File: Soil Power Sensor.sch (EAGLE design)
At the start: 99 parts, among them J1 12401832E402A, U10 TPS7A20330PDBVR, U11 TPS60403DBVR, U12 REF1933AIDDCR, U13 TLV1117LV33DCYR, U14 FSA2466UMX, U2 FT234XD-R, U3 MAX9944ATA+T, U4 ESP32-C3-MINI-1-N4, U5 LTC6362CDDPBF, U6 LTC6362CDDPBF, U7 INA296A5, U8 MAX11201AEUB+, U9 MAX11201AEUB+, X1 SMA-142-0701-801/806

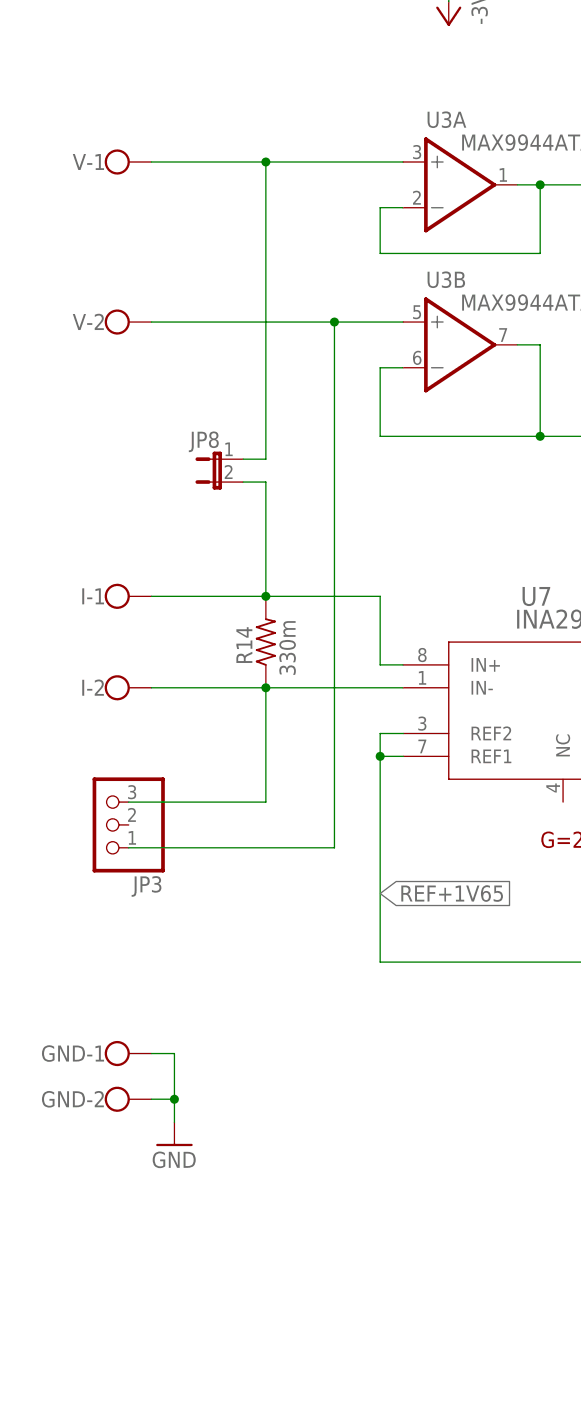
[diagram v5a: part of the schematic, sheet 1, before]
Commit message: Fixed in-situ load connections
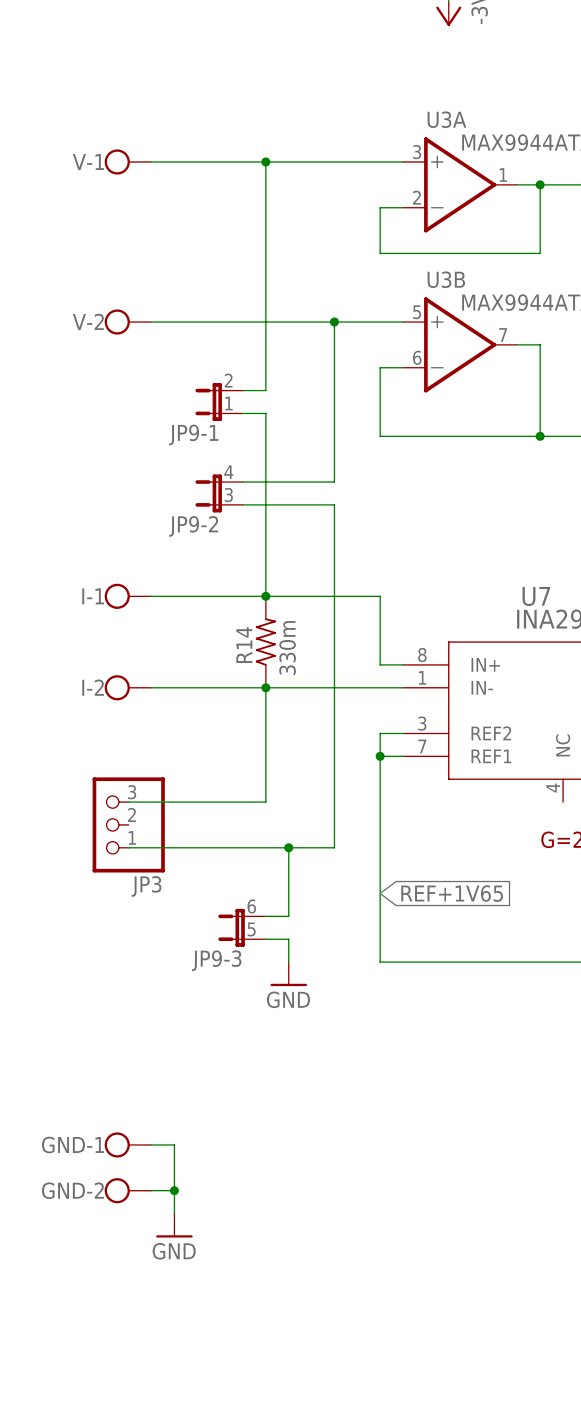
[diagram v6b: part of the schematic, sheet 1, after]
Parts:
- removed JP8: (no value), jumper:JP1E
- added JP9: (no value), jumper:JP3QE
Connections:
- new net N$48: JP3.1, JP9-2.1, JP9-3.2
- net GND: now also JP9-3.1
- net N$1: now also JP9-1.2; no longer JP8.1
- net N$45: now also JP9-1.1; no longer JP8.2
- net N$46: now also JP9-2.2; no longer JP3.1
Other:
- moved on the sheet: GND-1, GND-2
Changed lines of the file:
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@@
 <part name="V" library="con-wago-500" library_urn="urn:adsk.eagle:library:195" deviceset="W237-102" device="" package3d_urn="urn:adsk.eagle:package:10688/1"/>
 <part name="I" library="con-wago-500" library_urn="urn:adsk.eagle:library:195" deviceset="W237-102" device="" package3d_urn="urn:adsk.eagle:package:10688/1"/>
-<part name="JP8" library="jumper" library_urn="urn:adsk.eagle:library:252" deviceset="JP1E" device="" package3d_urn="urn:adsk.eagle:package:15455/1"/>
 <part name="JP2" library="jumper" library_urn="urn:adsk.eagle:library:252" deviceset="JP2E" device="" package3d_urn="urn:adsk.eagle:package:15452/1"/>
 <part name="P+7" library="supply1" library_urn="urn:adsk.eagle:library:371" deviceset="VCC" device=""/>
+<part name="JP9" library="jumper" library_urn="urn:adsk.eagle:library:252" deviceset="JP3QE" device="" package3d_urn="urn:adsk.eagle:package:15460/1"/>
+<part name="GND26" library="supply1" library_urn="urn:adsk.eagle:library:371" deviceset="GND" device=""/>
 </parts>
 <sheets>
@@
 <attribute name="TP_SIGNAL_NAME" x="95.25" y="97.79" size="1.778" layer="97"/>
 </instance>
-<instance part="GND" gate="-1" x="15.24" y="55.88" smashed="yes">
-<attribute name="NAME" x="15.24" y="56.769" size="1.778" layer="95" rot="R180"/>
-</instance>
-<instance part="GND" gate="-2" x="15.24" y="50.8" smashed="yes">
-<attribute name="VALUE" x="12.7" y="47.117" size="1.778" layer="96"/>
-<attribute name="NAME" x="15.24" y="51.689" size="1.778" layer="95" rot="R180"/>
-</instance>
-<instance part="GND42" gate="1" x="22.86" y="45.72" smashed="yes">
-<attribute name="VALUE" x="20.32" y="43.18" size="1.778" layer="96"/>
+<instance part="GND" gate="-1" x="15.24" y="45.72" smashed="yes">
+<attribute name="NAME" x="15.24" y="46.609" size="1.778" layer="95" rot="R180"/>
+</instance>
+<instance part="GND" gate="-2" x="15.24" y="40.64" smashed="yes">
+<attribute name="VALUE" x="12.7" y="36.957" size="1.778" layer="96"/>
+<attribute name="NAME" x="15.24" y="41.529" size="1.778" layer="95" rot="R180"/>
+</instance>
+<instance part="GND42" gate="1" x="22.86" y="35.56" smashed="yes">
+<attribute name="VALUE" x="20.32" y="33.02" size="1.778" layer="96"/>
 </instance>
 <instance part="JP3" gate="A" x="15.24" y="81.28" smashed="yes" rot="R180">
@@
 <attribute name="NAME" x="15.24" y="97.409" size="1.778" layer="95" rot="R180"/>
 </instance>
-<instance part="JP8" gate="A" x="27.94" y="121.92" smashed="yes" rot="MR270">
-<attribute name="NAME" x="27.94" y="123.19" size="1.778" layer="95" rot="MR0"/>
-<attribute name="VALUE" x="27.94" y="116.205" size="1.778" layer="96" rot="MR0"/>
+<instance part="JP9" gate="-1" x="27.94" y="127" smashed="yes" rot="R90">
+<attribute name="NAME" x="27.94" y="125.73" size="1.778" layer="95" rot="R180"/>
+<attribute name="VALUE" x="27.94" y="132.715" size="1.778" layer="96" rot="R180"/>
+</instance>
+<instance part="JP9" gate="-2" x="27.94" y="116.84" smashed="yes" rot="R90">
+<attribute name="NAME" x="27.94" y="115.57" size="1.778" layer="95" rot="R180"/>
+<attribute name="VALUE" x="27.94" y="122.555" size="1.778" layer="96" rot="R180"/>
+</instance>
+<instance part="JP9" gate="-3" x="30.48" y="68.58" smashed="yes" rot="R90">
+<attribute name="NAME" x="30.48" y="67.31" size="1.778" layer="95" rot="R180"/>
+<attribute name="VALUE" x="30.48" y="74.295" size="1.778" layer="96" rot="R180"/>
+</instance>
+<instance part="GND26" gate="1" x="35.56" y="63.5" smashed="yes">
+<attribute name="VALUE" x="33.02" y="60.96" size="1.778" layer="96"/>
 </instance>
 </instances>
@@
 <pinref part="GND" gate="-2" pin="KL"/>
 <pinref part="GND42" gate="1" pin="GND"/>
-<wire x1="20.32" y1="50.8" x2="22.86" y2="50.8" width="0.1524" layer="91"/>
-<wire x1="22.86" y1="50.8" x2="22.86" y2="48.26" width="0.1524" layer="91"/>
+<wire x1="20.32" y1="40.64" x2="22.86" y2="40.64" width="0.1524" layer="91"/>
+<wire x1="22.86" y1="40.64" x2="22.86" y2="38.1" width="0.1524" layer="91"/>
 <pinref part="GND" gate="-1" pin="KL"/>
-<wire x1="22.86" y1="50.8" x2="22.86" y2="55.88" width="0.1524" layer="91"/>
-<wire x1="22.86" y1="55.88" x2="20.32" y2="55.88" width="0.1524" layer="91"/>
-<junction x="22.86" y="50.8"/>
+<wire x1="22.86" y1="40.64" x2="22.86" y2="45.72" width="0.1524" layer="91"/>
+<wire x1="22.86" y1="45.72" x2="20.32" y2="45.72" width="0.1524" layer="91"/>
+<junction x="22.86" y="40.64"/>
+</segment>
+<segment>
+<pinref part="JP9" gate="-3" pin="1"/>
+<pinref part="GND26" gate="1" pin="GND"/>
+<wire x1="33.02" y1="68.58" x2="35.56" y2="68.58" width="0.1524" layer="91"/>
+<wire x1="35.56" y1="68.58" x2="35.56" y2="66.04" width="0.1524" layer="91"/>
 </segment>
 </net>
@@
 <wire x1="20.32" y1="106.68" x2="33.02" y2="106.68" width="0.1524" layer="91"/>
 <junction x="33.02" y="106.68"/>
-<pinref part="JP8" gate="A" pin="2"/>
-<wire x1="30.48" y1="119.38" x2="33.02" y2="119.38" width="0.1524" layer="91"/>
-<wire x1="33.02" y1="119.38" x2="33.02" y2="106.68" width="0.1524" layer="91"/>
+<wire x1="33.02" y1="127" x2="33.02" y2="106.68" width="0.1524" layer="91"/>
+<pinref part="JP9" gate="-1" pin="1"/>
+<wire x1="30.48" y1="127" x2="33.02" y2="127" width="0.1524" layer="91"/>
 </segment>
 </net>
@@
 <pinref part="V" gate="-1" pin="KL"/>
 <wire x1="48.26" y1="154.94" x2="33.02" y2="154.94" width="0.1524" layer="91"/>
-<pinref part="JP8" gate="A" pin="1"/>
 <wire x1="33.02" y1="154.94" x2="20.32" y2="154.94" width="0.1524" layer="91"/>
-<wire x1="30.48" y1="121.92" x2="33.02" y2="121.92" width="0.1524" layer="91"/>
-<wire x1="33.02" y1="121.92" x2="33.02" y2="154.94" width="0.1524" layer="91"/>
+<wire x1="33.02" y1="129.54" x2="33.02" y2="154.94" width="0.1524" layer="91"/>
 <junction x="33.02" y="154.94"/>
+<pinref part="JP9" gate="-1" pin="2"/>
+<wire x1="30.48" y1="129.54" x2="33.02" y2="129.54" width="0.1524" layer="91"/>
 </segment>
 </net>
@@
 <pinref part="V" gate="-2" pin="KL"/>
 <wire x1="20.32" y1="137.16" x2="40.64" y2="137.16" width="0.1524" layer="91"/>
+<junction x="40.64" y="137.16"/>
+<wire x1="40.64" y1="119.38" x2="40.64" y2="137.16" width="0.1524" layer="91"/>
+<pinref part="JP9" gate="-2" pin="2"/>
+<wire x1="30.48" y1="119.38" x2="40.64" y2="119.38" width="0.1524" layer="91"/>
+</segment>
+</net>
+<net name="N$48" class="0">
+<segment>
+<wire x1="35.56" y1="78.74" x2="40.64" y2="78.74" width="0.1524" layer="91"/>
+<pinref part="JP9" gate="-3" pin="2"/>
+<wire x1="33.02" y1="71.12" x2="35.56" y2="71.12" width="0.1524" layer="91"/>
+<wire x1="35.56" y1="71.12" x2="35.56" y2="78.74" width="0.1524" layer="91"/>
+<junction x="35.56" y="78.74"/>
 <pinref part="JP3" gate="A" pin="1"/>
-<wire x1="17.78" y1="78.74" x2="40.64" y2="78.74" width="0.1524" layer="91"/>
-<wire x1="40.64" y1="78.74" x2="40.64" y2="137.16" width="0.1524" layer="91"/>
-<junction x="40.64" y="137.16"/>
-</segment>
-</net>
+<wire x1="17.78" y1="78.74" x2="35.56" y2="78.74" width="0.1524" layer="91"/>
+<pinref part="JP9" gate="-2" pin="1"/>
+<wire x1="30.48" y1="116.84" x2="40.64" y2="116.84" width="0.1524" layer="91"/>
+<wire x1="40.64" y1="116.84" x2="40.64" y2="78.74" width="0.1524" layer="91"/>
+</segment>
+</net>

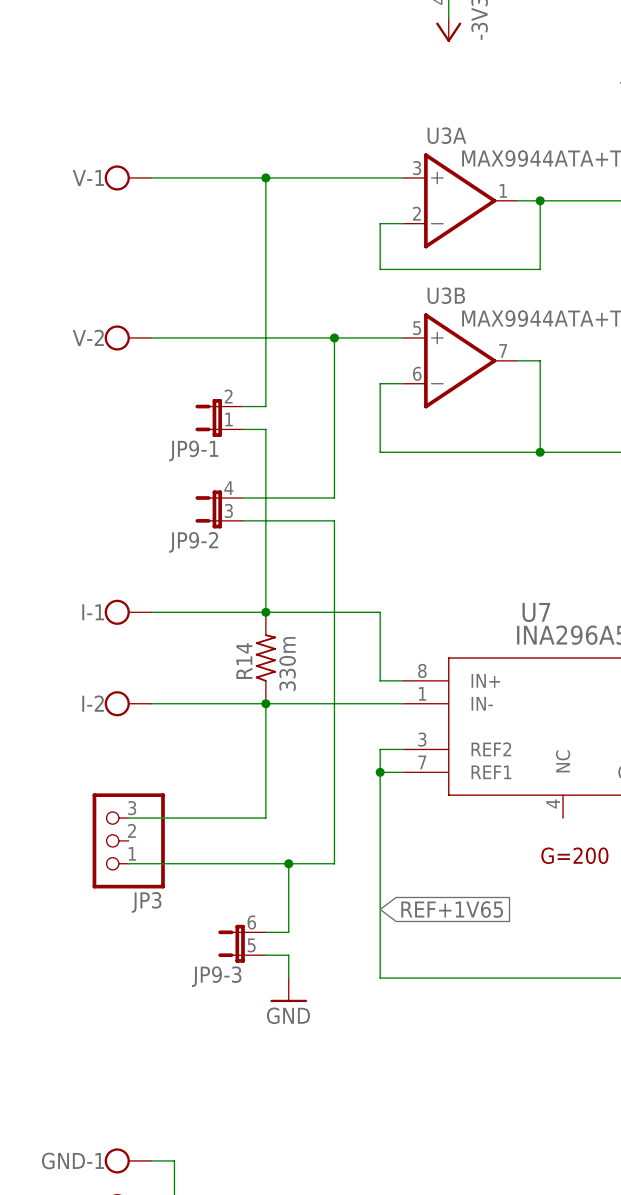
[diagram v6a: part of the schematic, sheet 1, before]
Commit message: Changed frames to include doc title and rev
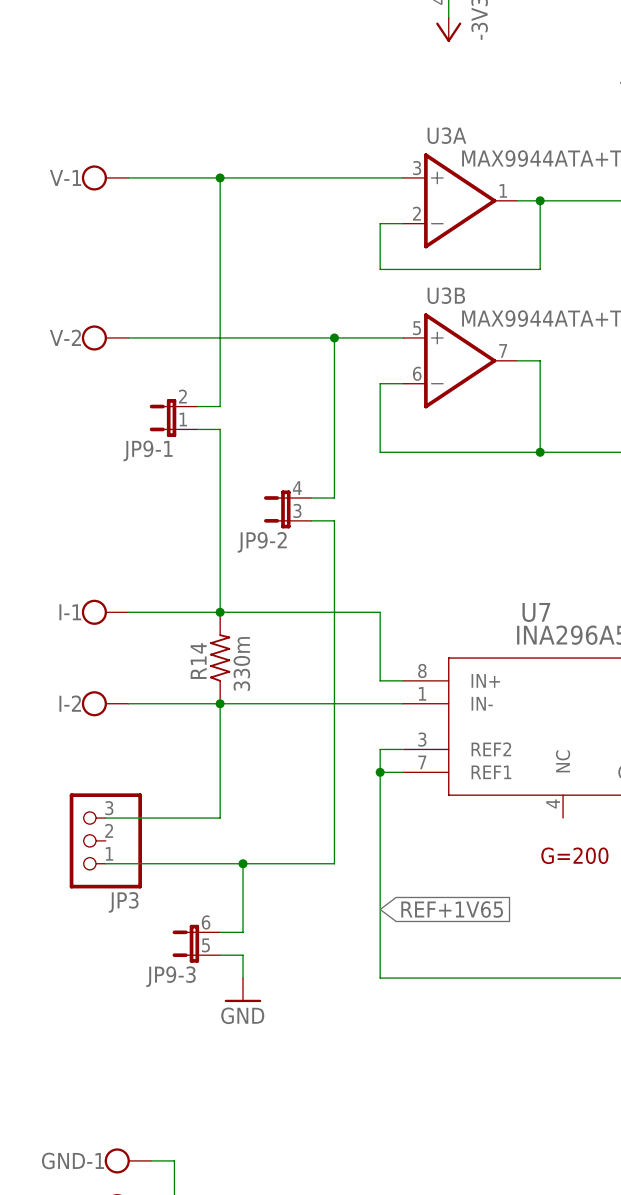
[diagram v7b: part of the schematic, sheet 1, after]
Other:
- moved on the sheet: I-1, I-2, JP3, JP9-1, JP9-2, JP9-3, R14, V-1, V-2
